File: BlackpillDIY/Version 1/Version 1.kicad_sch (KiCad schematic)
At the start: 15 parts, among them J1 Left Header, J2 Right Header, J3 Debug, SW1 Reset Switch, U1 STM32F411CCUx, Y1 Crystal_GND24

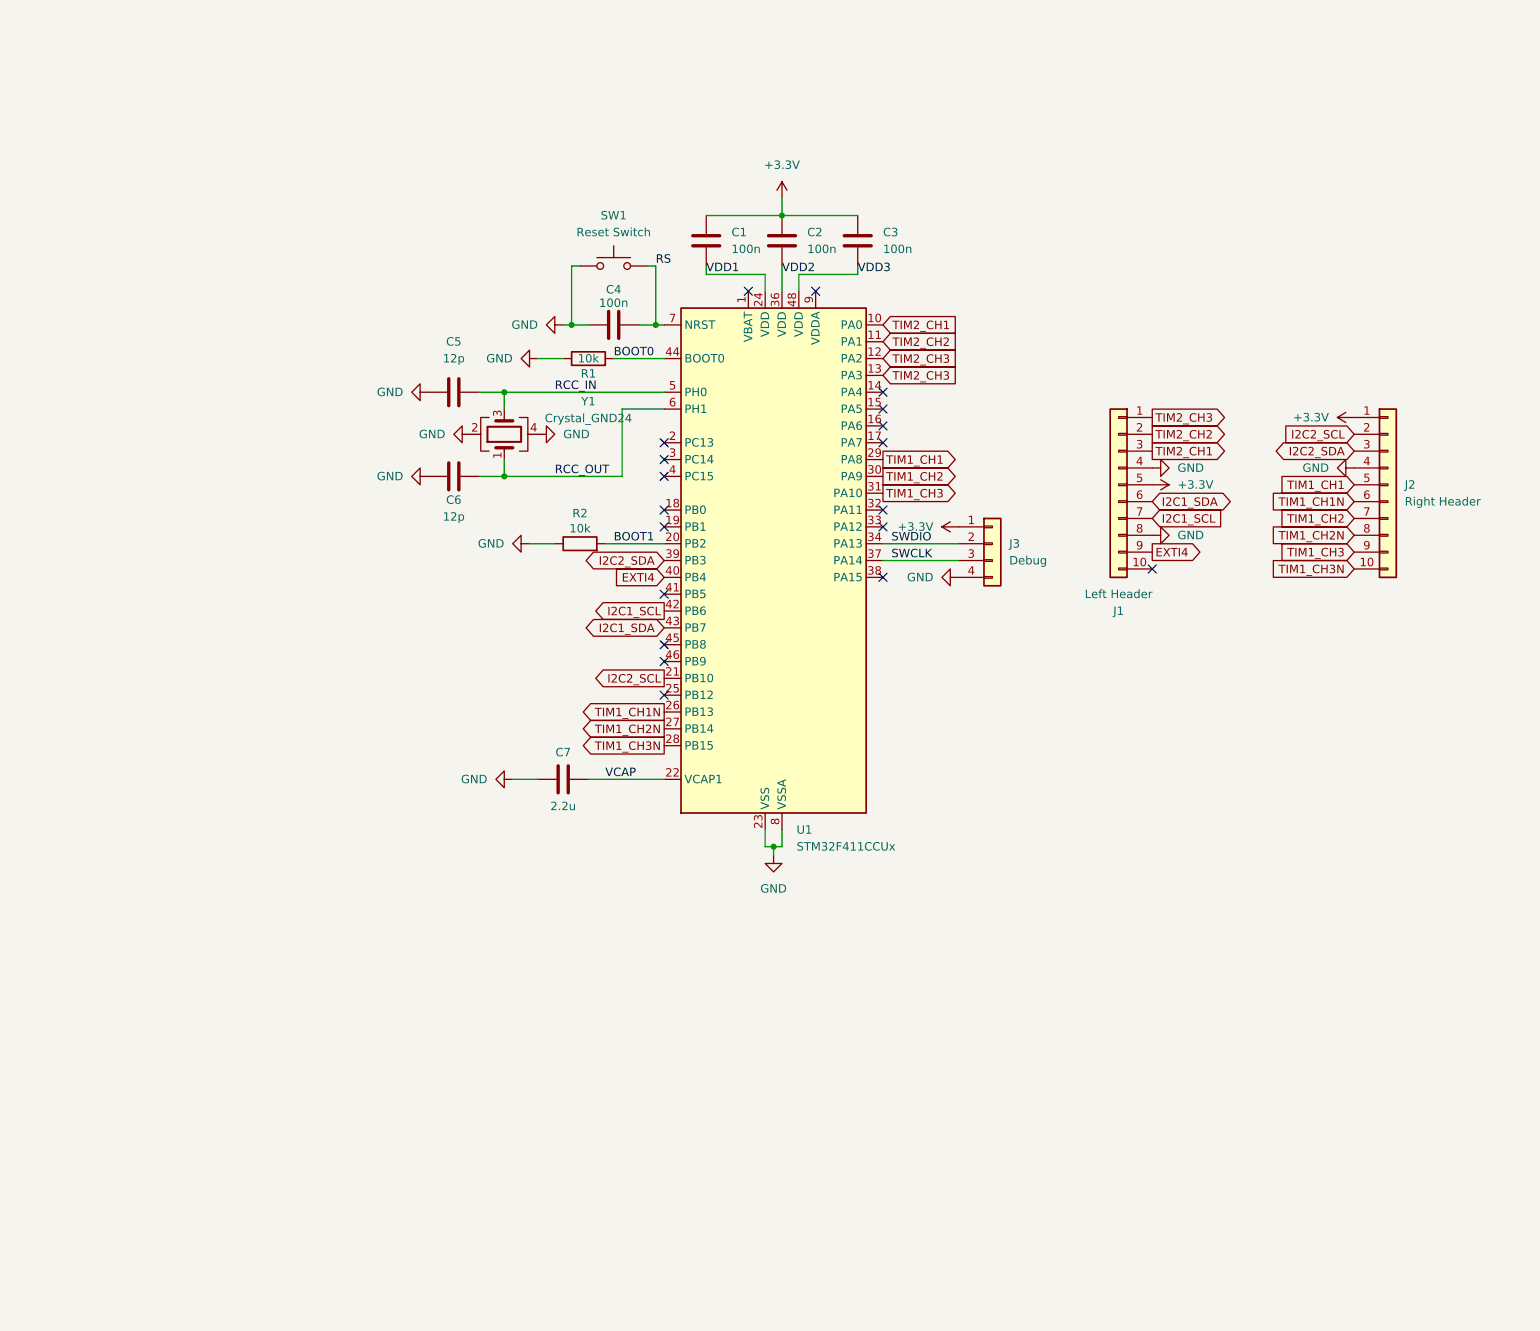
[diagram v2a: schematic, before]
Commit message: Added breakouts for ESP Ublock and LIS.
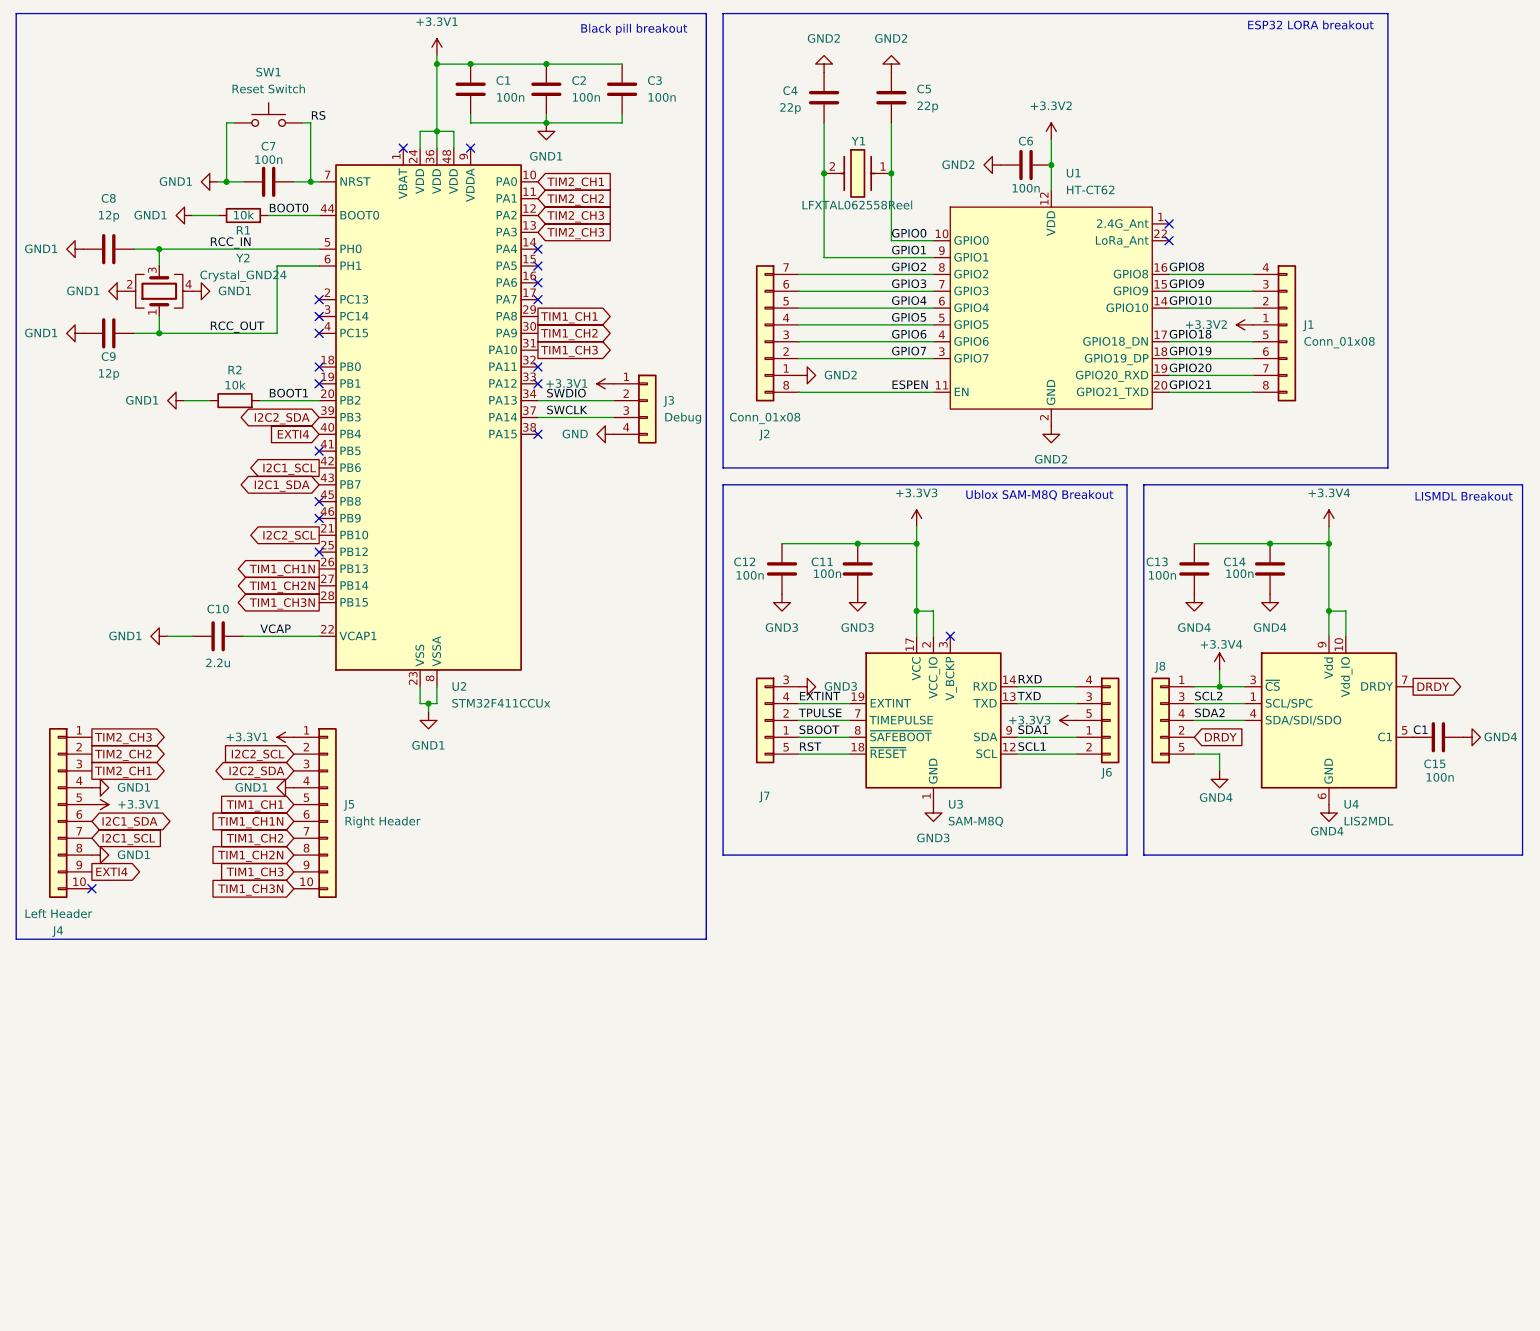
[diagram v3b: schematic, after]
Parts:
- added C11, C12, C13, C14, C15, C6: 100n, Capacitor_THT:C_Disc_D5.0mm_W2.5mm_P5.00mm, symbol Device:C
- added C4, C5: 22p, Capacitor_THT:C_Disc_D5.0mm_W2.5mm_P5.00mm, symbol Device:C
- added J1, J2: Conn_01x08, Connector_PinHeader_2.54mm:PinHeader_1x08_P2.54mm_Vertical, symbol Connector_Generic:Conn_01x08
- added J6, J7, J8: Conn_01x05, Connector_PinHeader_2.54mm:PinHeader_1x05_P2.54mm_Vertical, symbol Connector_Generic:Conn_01x05
- added U1: HT-CT62, RF_Module:Heltec_HT-CT62, symbol RF_Module:HT-CT62
- added U3: SAM-M8Q, RF_GPS:ublox_SAM-M8Q, symbol RF_GPS:SAM-M8Q
- added U4: LIS2MDL, Package_LGA:LGA-12_2x2mm_P0.5mm, symbol Sensor_Magnetic:LIS2MDL
- added Y1: LFXTAL062558Reel, LIB_LFXTAL062558Reel:LFXTAL062558Reel, symbol LFXTAL062558Reel:LFXTAL062558Reel
- renumbered C7 to C10, C4 to C7, C5 to C8, C6 to C9, J1 to J4, J2 to J5, U1 to U2, Y1 to Y2
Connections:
- net GND: no longer C10.1, C7.1, C8.1, C9.1, J4.4 (Pin_4), J4.8 (Pin_8), J5.4 (Pin_4), R1.1, R2.1, SW1.1, U2.23 (VSS), U2.35 (VSS), U2.47 (VSS), U2.49 (VSS), U2.8 (VSSA), Y2.2, Y2.4
- net +3.3V renamed +3.3V1
- net +3.3V1: now also U2.24 (VDD), U2.36 (VDD), U2.48 (VDD)
- net VDD1 renamed GND1
- net GND1: now also C10.1, C2.2, C3.2, C7.1, C8.1, C9.1, J4.4 (Pin_4), J4.8 (Pin_8), J5.4 (Pin_4), R1.1, R2.1, SW1.1, U2.23 (VSS), U2.35 (VSS), U2.47 (VSS), U2.49 (VSS), U2.8 (VSSA), Y2.2, Y2.4; no longer U2.24 (VDD)
- removed net VDD2: C2.2, U2.36 (VDD)
- removed net VDD3: C3.2, U2.48 (VDD)
- new net +3.3V2: C6.1, J1.1 (Pin_1), U1.12 (VDD)
- new net +3.3V3: C11.1, C12.1, J6.5 (Pin_5), U3.17 (VCC), U3.2 (VCC_IO)
- new net +3.3V4: C13.1, C14.1, J8.1 (Pin_1), U4.10 (Vdd_IO), U4.3 (~{CS}), U4.9 (Vdd)
- new net C1: C15.1, U4.5 (C1)
- new net DRDY: J8.2 (Pin_2), U4.7 (DRDY)
- new net ESPEN: J2.8 (Pin_8), U1.11 (EN)
- new net EXTINT: J7.4 (Pin_4), U3.19 (EXTINT)
- new net GND2: C4.2, C5.2, C6.2, J2.1 (Pin_1), U1.13 (GND), U1.2 (GND), U1.21 (GND)
- new net GND3: C11.2, C12.2, J7.3 (Pin_3), U3.1 (GND), U3.10 (GND), U3.11 (GND), U3.15 (GND), U3.16 (GND), U3.20 (GND), U3.4 (GND), U3.5 (GND), U3.6 (GND)
- new net GND4: C13.2, C14.2, C15.2, J8.5 (Pin_5), U4.6 (GND), U4.8 (GND)
- new net GPIO0: C5.1, U1.10 (GPIO0), Y1.1
- new net GPIO1: C4.1, U1.9 (GPIO1), Y1.2 (CRYSTAL_2)
- new net GPIO10: J1.2 (Pin_2), U1.14 (GPIO10)
- new net GPIO18: J1.5 (Pin_5), U1.17 (GPIO18_DN)
- new net GPIO19: J1.6 (Pin_6), U1.18 (GPIO19_DP)
- new net GPIO2: J2.7 (Pin_7), U1.8 (GPIO2)
- new net GPIO20: J1.7 (Pin_7), U1.19 (GPIO20_RXD)
- new net GPIO21: J1.8 (Pin_8), U1.20 (GPIO21_TXD)
- new net GPIO3: J2.6 (Pin_6), U1.7 (GPIO3)
- new net GPIO4: J2.5 (Pin_5), U1.6 (GPIO4)
- new net GPIO5: J2.4 (Pin_4), U1.5 (GPIO5)
- new net GPIO6: J2.3 (Pin_3), U1.4 (GPIO6)
- new net GPIO7: J2.2 (Pin_2), U1.3 (GPIO7)
- new net GPIO8: J1.4 (Pin_4), U1.16 (GPIO8)
- new net GPIO9: J1.3 (Pin_3), U1.15 (GPIO9)
- new net RST: J7.5 (Pin_5), U3.18 (~{RESET})
- new net RXD: J6.4 (Pin_4), U3.14 (RXD)
- new net SBOOT: J7.1 (Pin_1), U3.8 (~{SAFEBOOT})
- new net SCL1: J6.2 (Pin_2), U3.12 (SCL)
- new net SCL2: J8.3 (Pin_3), U4.1 (SCL/SPC)
- new net SDA1: J6.1 (Pin_1), U3.9 (SDA)
- new net SDA2: J8.4 (Pin_4), U4.4 (SDA/SDI/SDO)
- new net TPULSE: J7.2 (Pin_2), U3.7 (TIMEPULSE)
- new net TXD: J6.3 (Pin_3), U3.13 (TXD)
- no-connect marks 19 -> 22
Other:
- note added: "Black pill breakout"
- note added: "ESP32 LORA breakout"
- note added: "LISMDL Breakout"
- note added: "Ublox SAM-M8Q Breakout"
- moved on the sheet: C1, C10, C2, C3, C7, C8, C9, J3, J4, J5, R1, R2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

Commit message: Added silkscreen and autoboot for esp
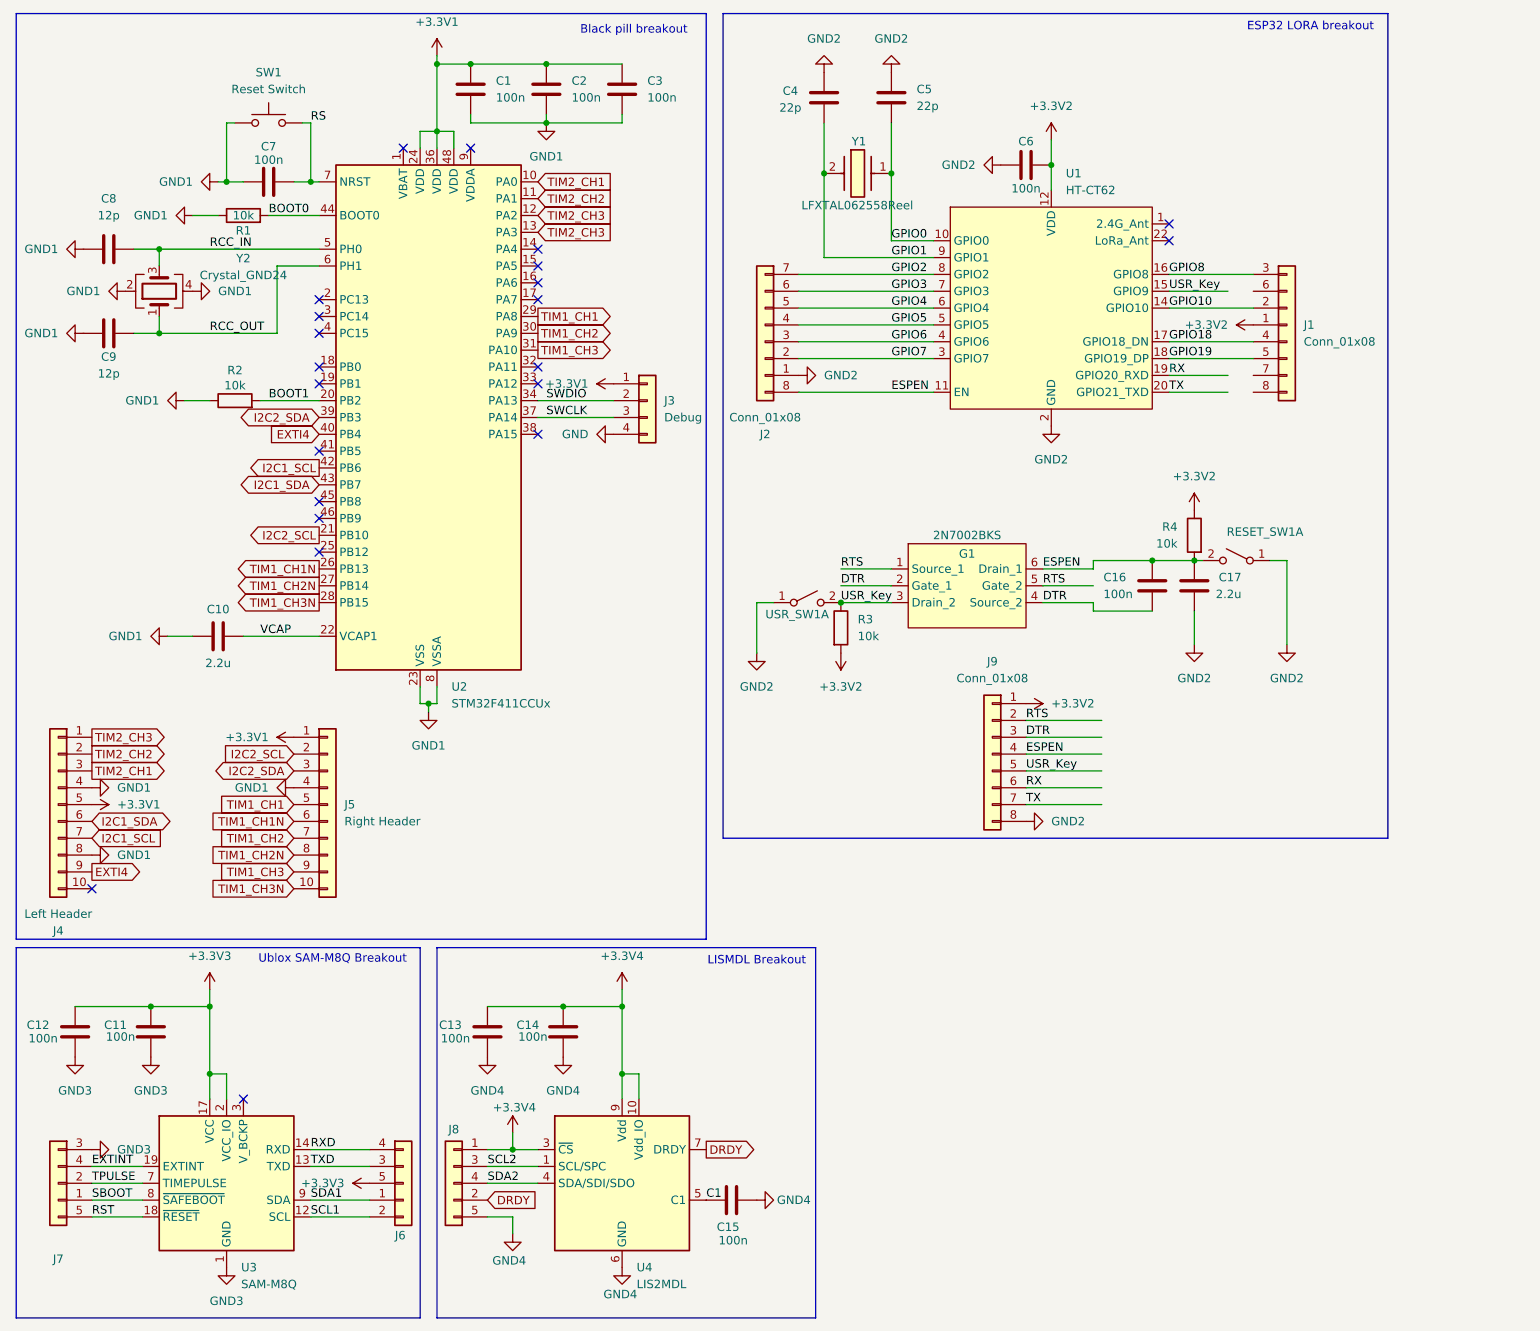
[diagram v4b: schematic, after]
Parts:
- added C16: 100n, Capacitor_THT:C_Disc_D5.0mm_W2.5mm_P5.00mm, symbol Device:C
- added C17: 2.2u, Capacitor_THT:CP_Radial_D5.0mm_P2.00mm, symbol Device:C
- added G1: 2N7002BKS, Package_TO_SOT_SMD:SOT-363_SC-70-6, symbol Custom:2N7002BKS
- added J9: Conn_01x08, Connector_PinHeader_2.54mm:PinHeader_1x08_P2.54mm_Vertical, symbol Connector_Generic:Conn_01x08
- added R3, R4: 10k, Resistor_THT:R_Axial_DIN0207_L6.3mm_D2.5mm_P10.16mm_Horizontal, symbol Device:R
- added RESET_SW1, USR_SW1: RESET_SW, Button_Switch_THT:SW_PUSH_6mm_H4.3mm, symbol Switch:SW_DPST_x2
- J1: footprint Connector_PinHeader_2.54mm:PinHeader_1x08_P2.54mm_Vertical -> Connector_PinHeader_2.54mm:PinHeader_1x05_P2.54mm_Vertical
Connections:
- net +3.3V2: now also J9.1 (Pin_1), R3.2, R4.1
- net ESPEN: now also C16.2, C17.2, G1.6 (Drain_1), J9.4 (Pin_4), R4.2, RESET_SW1.2 (B)
- net GND2: now also C17.1, J9.8 (Pin_8), RESET_SW1.1 (A), USR_SW1.1 (A)
- net GPIO18: now also J1.4 (Pin_4); no longer J1.5 (Pin_5)
- net GPIO19: now also J1.5 (Pin_5); no longer J1.6 (Pin_6)
- net GPIO8: now also J1.3 (Pin_3); no longer J1.4 (Pin_4)
- net GPIO20: no longer names the net of J1.7 (Pin_7)
- net GPIO20: no longer U1.19 (GPIO20_RXD)
- net GPIO21: no longer names the net of J1.8 (Pin_8)
- net GPIO21: no longer U1.20 (GPIO21_TXD)
- net GPIO9 renamed USR_Key
- net USR_Key: now also G1.3 (Drain_2), J9.5 (Pin_5), R3.1, USR_SW1.2 (B); no longer J1.3 (Pin_3)
- new net DTR: C16.1, G1.2 (Gate_1), G1.4 (Source_2), J9.3 (Pin_3)
- new net RTS: G1.1 (Source_1), G1.5 (Gate_2), J9.2 (Pin_2)
- new net RX: J9.6 (Pin_6), U1.19 (GPIO20_RXD)
- new net TX: J9.7 (Pin_7), U1.20 (GPIO21_TXD)
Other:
- moved on the sheet: C11, C12, C13, C14, C15, J6, J7, J8, U3, U4
